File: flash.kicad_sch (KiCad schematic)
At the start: 1 part, among them U1 MIMXRT1052CVJ5B

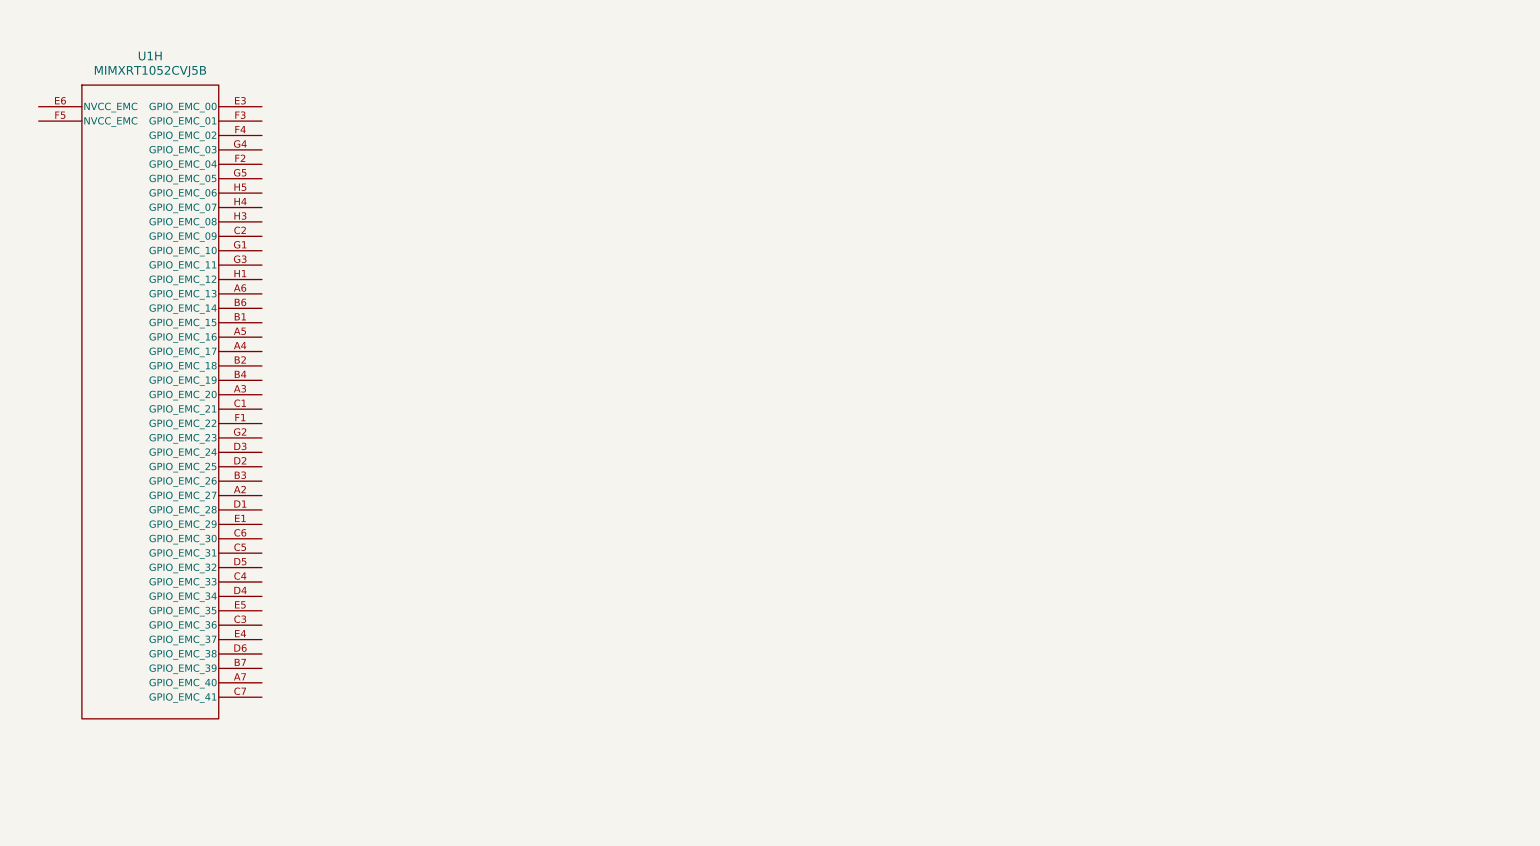
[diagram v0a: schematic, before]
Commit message: assign pin functions and started spe
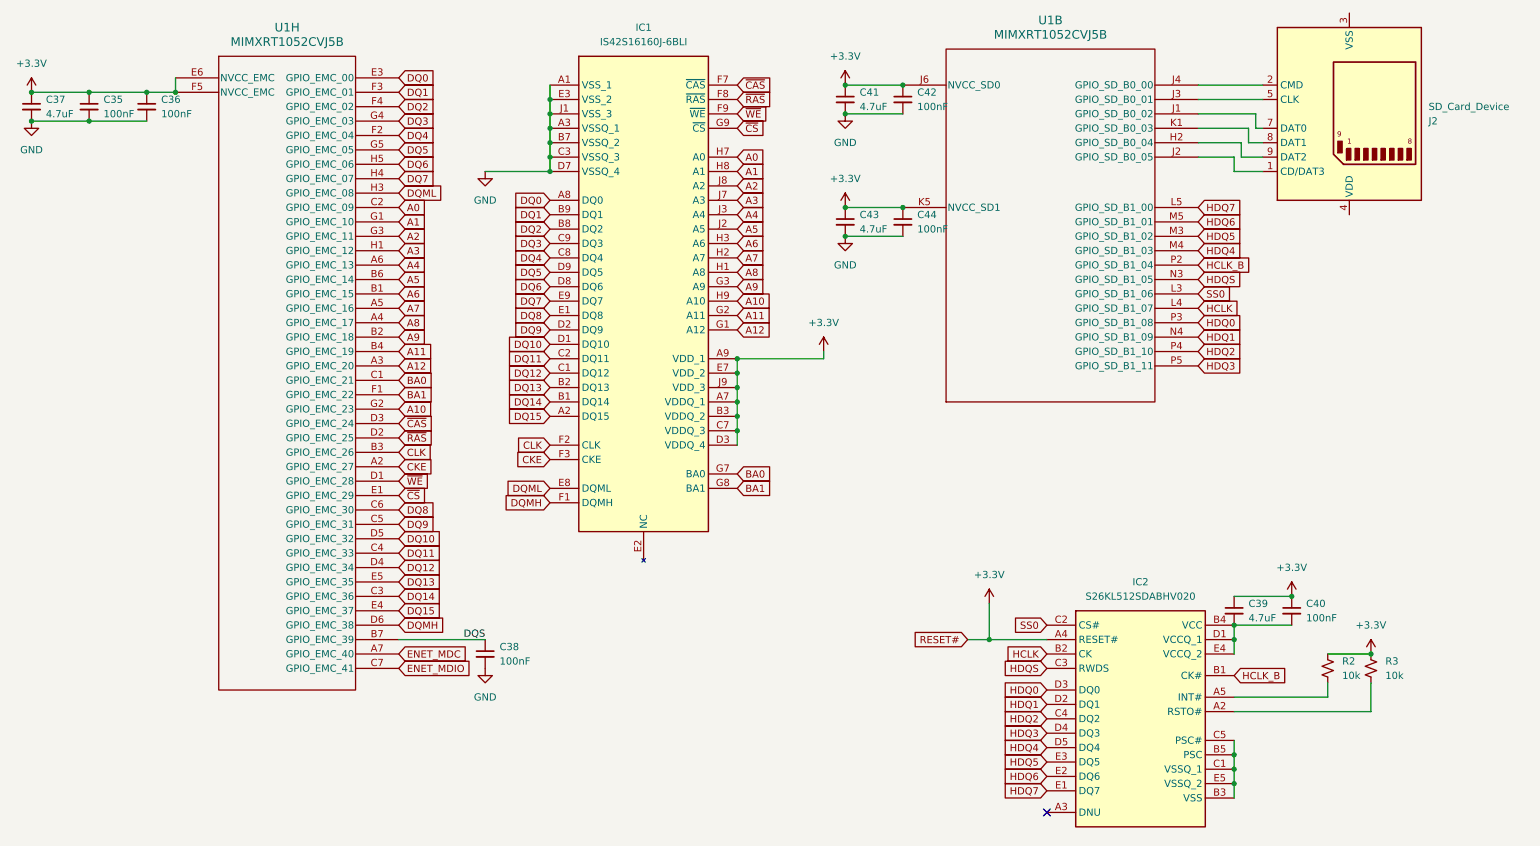
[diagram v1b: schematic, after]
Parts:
- added C35, C36, C38, C40, C42, C44: 100nF, symbol Device:C_Small
- added C37, C39, C41, C43: 4.7uF, symbol Device:C_Small
- added IC1: IS42S16160J-6BLI, BGA54C80P9X9_800X800X120, symbol IS42S16160J-6BLI:IS42S16160J-6BLI
- added IC2: S26KL512SDABHV020, BGA24C100P5X5_600X800X100, symbol S26KS512SDPBHV020:S26KS512SDPBHV020
- added J2: SD_Card_Device, symbol Connector:SD_Card_Device
- added R2, R3: 10k, symbol Device:R_Small_US
- added unit 2 of U1
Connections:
- net CKE: now reaches U1.A2 (GPIO_EMC_27)
- net CKE: now also IC1.F3 (CKE)
- net A12: now reaches U1.A3 (GPIO_EMC_20)
- net A12: now also IC1.G1 (A12)
- net A8: now reaches U1.A4 (GPIO_EMC_17)
- net A8: now also IC1.H1 (A8)
- net A7: now reaches U1.A5 (GPIO_EMC_16)
- net A7: now also IC1.H2 (A7)
- net A4: now reaches U1.A6 (GPIO_EMC_13)
- net A4: now also IC1.J3 (A4)
- net ENET_MDC: now reaches U1.A7 (GPIO_EMC_40)
- net A6: now reaches U1.B1 (GPIO_EMC_15)
- net A6: now also IC1.H3 (A6)
- net A9: now reaches U1.B2 (GPIO_EMC_18)
- net A9: now also IC1.G3 (A9)
- net CLK: now reaches U1.B3 (GPIO_EMC_26)
- net CLK: now also IC1.F2 (CLK)
- net A11: now reaches U1.B4 (GPIO_EMC_19)
- net A11: now also IC1.G2 (A11)
- net A5: now reaches U1.B6 (GPIO_EMC_14)
- net A5: now also IC1.J2 (A5)
- net DQS: now reaches U1.B7 (GPIO_EMC_39)
- net DQS: now also C38.1
- net BA0: now reaches U1.C1 (GPIO_EMC_21)
- net BA0: now also IC1.G7 (BA0)
- net A0: now reaches U1.C2 (GPIO_EMC_09)
- net A0: now also IC1.H7 (A0)
- net DQ14: now reaches U1.C3 (GPIO_EMC_36)
- net DQ14: now also IC1.B1 (DQ14)
- net DQ11: now reaches U1.C4 (GPIO_EMC_33)
- net DQ11: now also IC1.C2 (DQ11)
- net DQ9: now reaches U1.C5 (GPIO_EMC_31)
- net DQ9: now also IC1.D2 (DQ9)
- net DQ8: now reaches U1.C6 (GPIO_EMC_30)
- net DQ8: now also IC1.E1 (DQ8)
- net ENET_MDIO: now reaches U1.C7 (GPIO_EMC_41)
- net ~{WE}: now reaches U1.D1 (GPIO_EMC_28)
- net ~{WE}: now also IC1.F9 (~{WE})
- net ~{RAS}: now reaches U1.D2 (GPIO_EMC_25)
- net ~{RAS}: now also IC1.F8 (~{RAS})
- net ~{CAS}: now reaches U1.D3 (GPIO_EMC_24)
- net ~{CAS}: now also IC1.F7 (~{CAS})
- net DQ12: now reaches U1.D4 (GPIO_EMC_34)
- net DQ12: now also IC1.C1 (DQ12)
- net DQ10: now reaches U1.D5 (GPIO_EMC_32)
- net DQ10: now also IC1.D1 (DQ10)
- net DQMH: now reaches U1.D6 (GPIO_EMC_38)
- net DQMH: now also IC1.F1 (DQMH)
- net ~{CS}: now reaches U1.E1 (GPIO_EMC_29)
- net ~{CS}: now also IC1.G9 (~{CS})
- net DQ0: now reaches U1.E3 (GPIO_EMC_00)
- net DQ0: now also IC1.A8 (DQ0)
- net DQ15: now reaches U1.E4 (GPIO_EMC_37)
- net DQ15: now also IC1.A2 (DQ15)
- net DQ13: now reaches U1.E5 (GPIO_EMC_35)
- net DQ13: now also IC1.B2 (DQ13)
- net +3.3V: now reaches U1.E6 (NVCC_EMC)
- net +3.3V: now also U1.F5 (NVCC_EMC), C35.1, C36.1, C37.1, C39.1, C40.1, C41.1, C42.1, C43.1, C44.1, IC1.A7 (VDDQ_1), IC1.A9 (VDD_1), IC1.B3 (VDDQ_2), IC1.C7 (VDDQ_3), IC1.D3 (VDDQ_4), IC1.E7 (VDD_2), IC1.J9 (VDD_3), IC2.A4 (RESET#), R2.1, R3.1, U1.J6 (NVCC_SD0), U1.K5 (NVCC_SD1)
- net BA1: now reaches U1.F1 (GPIO_EMC_22)
- net BA1: now also IC1.G8 (BA1)
- net DQ4: now reaches U1.F2 (GPIO_EMC_04)
- net DQ4: now also IC1.C8 (DQ4)
- net DQ1: now reaches U1.F3 (GPIO_EMC_01)
- net DQ1: now also IC1.B9 (DQ1)
- net DQ2: now reaches U1.F4 (GPIO_EMC_02)
- net DQ2: now also IC1.B8 (DQ2)
- net A1: now reaches U1.G1 (GPIO_EMC_10)
- net A1: now also IC1.H8 (A1)
- net A10: now reaches U1.G2 (GPIO_EMC_23)
- net A10: now also IC1.H9 (A10)
- net A2: now reaches U1.G3 (GPIO_EMC_11)
- net A2: now also IC1.J8 (A2)
- net DQ3: now reaches U1.G4 (GPIO_EMC_03)
- net DQ3: now also IC1.C9 (DQ3)
- net DQ5: now reaches U1.G5 (GPIO_EMC_05)
- net DQ5: now also IC1.D9 (DQ5)
- net A3: now reaches U1.H1 (GPIO_EMC_12)
- net A3: now also IC1.J7 (A3)
- net DQML: now reaches U1.H3 (GPIO_EMC_08)
- net DQML: now also IC1.E8 (DQML)
- net DQ7: now reaches U1.H4 (GPIO_EMC_07)
- net DQ7: now also IC1.E9 (DQ7)
- net DQ6: now reaches U1.H5 (GPIO_EMC_06)
- net DQ6: now also IC1.D8 (DQ6)
- new net: IC2.A5 (INT#), R2.2
- new net: IC2.A2 (RSTO#), R3.2
- new net: IC2.B3 (VSS), IC2.B5 (PSC), IC2.C1 (VSSQ_1), IC2.C5 (PSC#), IC2.E5 (VSSQ_2)
- new net: C39.2, C40.2, IC2.B4 (VCC), IC2.D1 (VCCQ_1), IC2.E4 (VCCQ_2)
- new net: J2.9 (DAT2), U1.H2 (GPIO_SD_B0_04)
- new net: J2.7 (DAT0), U1.J1 (GPIO_SD_B0_02)
- new net: J2.1 (CD/DAT3), U1.J2 (GPIO_SD_B0_05)
- new net: J2.5 (CLK), U1.J3 (GPIO_SD_B0_01)
- new net: J2.2 (CMD), U1.J4 (GPIO_SD_B0_00)
- new net: J2.8 (DAT1), U1.K1 (GPIO_SD_B0_03)
- new net: J2.3 (VSS), J2.6 (VSS)
- new net GND: C35.2, C36.2, C37.2, C38.2, C41.2, C42.2, C43.2, C44.2, IC1.A1 (VSS_1), IC1.A3 (VSSQ_1), IC1.B7 (VSSQ_2), IC1.C3 (VSSQ_3), IC1.D7 (VSSQ_4), IC1.E3 (VSS_2), IC1.J1 (VSS_3)
- new net HCLK: IC2.B2 (CK), U1.L4 (GPIO_SD_B1_07)
- new net HCLK_B: IC2.B1 (CK#), U1.P2 (GPIO_SD_B1_04)
- new net HDQ0: IC2.D3 (DQ0), U1.P3 (GPIO_SD_B1_08)
- new net HDQ1: IC2.D2 (DQ1), U1.N4 (GPIO_SD_B1_09)
- new net HDQ2: IC2.C4 (DQ2), U1.P4 (GPIO_SD_B1_10)
- new net HDQ3: IC2.D4 (DQ3), U1.P5 (GPIO_SD_B1_11)
- new net HDQ4: IC2.D5 (DQ4), U1.M4 (GPIO_SD_B1_03)
- new net HDQ5: IC2.E3 (DQ5), U1.M3 (GPIO_SD_B1_02)
- new net HDQ6: IC2.E2 (DQ6), U1.M5 (GPIO_SD_B1_01)
- new net HDQ7: IC2.E1 (DQ7), U1.L5 (GPIO_SD_B1_00)
- new net HDQS: IC2.C3 (RWDS), U1.N3 (GPIO_SD_B1_05)
- new net SS0: IC2.C2 (CS#), U1.L3 (GPIO_SD_B1_06)
- no-connect marks 0 -> 1
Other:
- moved on the sheet: U1H

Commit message: finished v1
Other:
- company: (none) -> Northeastern University
- title: (none) -> RT1050 DevBoard for Project Horizon
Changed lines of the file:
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@@
 	(generator_version "8.0")
 	(paper "A4")
+	(title_block
+		(title "RT1050 DevBoard for Project Horizon")
+		(rev "v1")
+		(company "Northeastern University")
+		(comment 1 "Built by Madhav Kapa")
+	)
 	(junction
 		(at 109.22 39.37)

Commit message: added load switches
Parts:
- C35, C36, C37, C38, C39, C40, C41, C42, C43, C44: footprint (none) -> Capacitor_SMD:C_0402_1005Metric
- J2: footprint (none) -> Connector_Card:microSD_HC_Molex_47219-2001
- R2, R3: footprint (none) -> Resistor_SMD:R_0402_1005Metric
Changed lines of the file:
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@@
 			)
 		)
-		(property "Footprint" ""
+		(property "Footprint" "Capacitor_SMD:C_0402_1005Metric"
 			(at 161.29 50.8 0)
 			(effects
@@
 			)
 		)
-		(property "Footprint" ""
+		(property "Footprint" "Capacitor_SMD:C_0402_1005Metric"
 			(at 171.45 50.8 0)
 			(effects
@@
 			)
 		)
-		(property "Footprint" ""
+		(property "Footprint" "Resistor_SMD:R_0402_1005Metric"
 			(at 246.38 129.54 0)
 			(effects
@@
 			)
 		)
-		(property "Footprint" ""
+		(property "Footprint" "Resistor_SMD:R_0402_1005Metric"
 			(at 254 129.54 0)
 			(effects
@@
 			)
 		)
-		(property "Footprint" ""
+		(property "Footprint" "Capacitor_SMD:C_0402_1005Metric"
 			(at 97.79 127 0)
 			(effects
@@
 			)
 		)
-		(property "Footprint" ""
+		(property "Footprint" "Capacitor_SMD:C_0402_1005Metric"
 			(at 229.87 119.38 0)
 			(effects
@@
 			)
 		)
-		(property "Footprint" ""
+		(property "Footprint" "Capacitor_SMD:C_0402_1005Metric"
 			(at 38.1 30.48 0)
 			(effects
@@
 			)
 		)
-		(property "Footprint" ""
+		(property "Footprint" "Capacitor_SMD:C_0402_1005Metric"
 			(at 161.29 29.21 0)
 			(effects
@@
 			)
 		)
-		(property "Footprint" ""
+		(property "Footprint" "Connector_Card:microSD_HC_Molex_47219-2001"
 			(at 250.19 31.75 0)
 			(effects
@@
 			)
 		)
-		(property "Footprint" ""
+		(property "Footprint" "Capacitor_SMD:C_0402_1005Metric"
 			(at 27.94 30.48 0)
 			(effects
@@
 			)
 		)
-		(property "Footprint" ""
+		(property "Footprint" "Capacitor_SMD:C_0402_1005Metric"
 			(at 171.45 29.21 0)
 			(effects
@@
 			)
 		)
-		(property "Footprint" ""
+		(property "Footprint" "Capacitor_SMD:C_0402_1005Metric"
 			(at 240.03 119.38 0)
 			(effects
@@
 			)
 		)
-		(property "Footprint" ""
+		(property "Footprint" "Capacitor_SMD:C_0402_1005Metric"
 			(at 17.78 30.48 0)
 			(effects

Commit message: save before sdram redesign
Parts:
- removed J2: SD_Card_Device, Connector_Card:microSD_HC_Molex_47219-2001, symbol Connector:SD_Card_Device
- C35, C36, C37, C38, C39, C40, C41, C42, C43, C44: footprint Capacitor_SMD:C_0402_1005Metric -> Capacitor_SMD:C_0201_0603Metric
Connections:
- net +3.3V: now also IC2.B4 (VCC), IC2.D1 (VCCQ_1), IC2.E4 (VCCQ_2)
- net GND: now also C39.2, C40.2, IC2.B3 (VSS), IC2.B5 (PSC), IC2.C1 (VSSQ_1), IC2.C5 (PSC#), IC2.E5 (VSSQ_2)
- no-connect marks 1 -> 7
